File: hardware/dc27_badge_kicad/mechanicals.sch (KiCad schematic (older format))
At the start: 6 parts

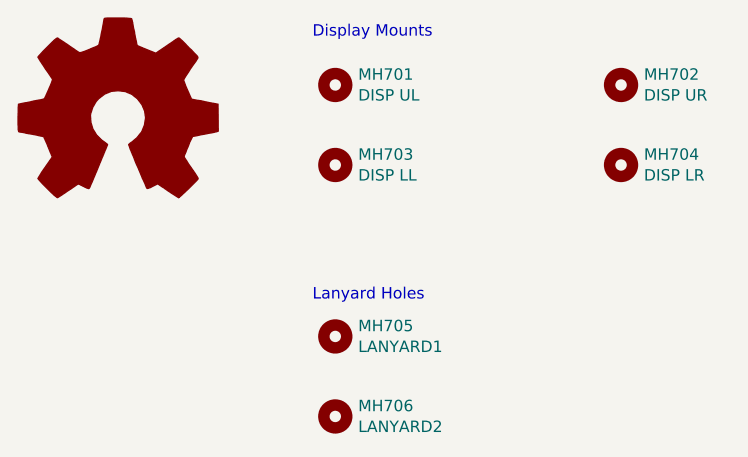
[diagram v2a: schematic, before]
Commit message: check in latest budget numbers, check in bombface graphics
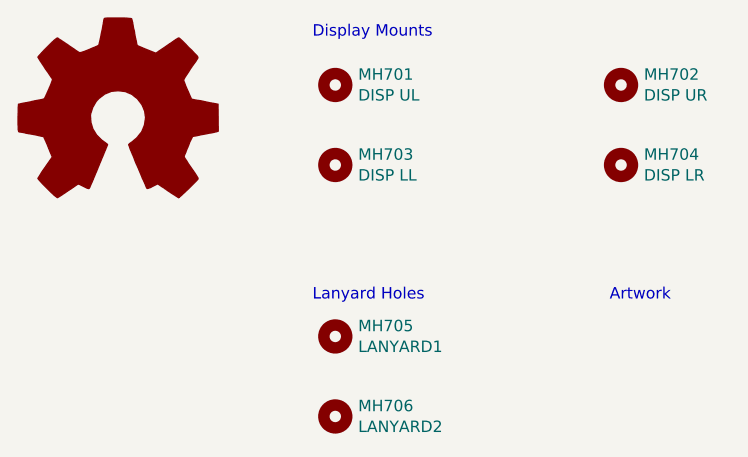
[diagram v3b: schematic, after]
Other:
- note added: "Artwork\n"
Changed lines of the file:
@@
 Text Notes 5650 4100 0    50   ~ 0
 Lanyard Holes\n
+Text Notes 6950 4100 0    50   ~ 0
+Artwork\n
 $EndSCHEMATC
